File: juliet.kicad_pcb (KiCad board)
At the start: 2 copper layers, 285.4 x 94.9 mm, 143 parts, among them J1 USB, J2 AVR_ISP_6, J3 JST, SW1 RESET, SW2 BOOT, U1 ATMEGA328-PU, Y1 16MHz

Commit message: Change bottom row layout options
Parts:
- removed 1.5u2_MX43: RCtrl, juliet:MX_PCB_150H
- added 1u_MX30: Fn2, juliet:MX, F.Cu at (147.6, 140.5)
- added 1u_MX37: Fn3, juliet:MX, F.Cu at (209.6, 140.5)
- added 2.25u_MX36: RSpace, juliet:MX_PCB_225H, F.Cu at (178.6, 140.5)
- added D37: 1N4148, Diode_THT:D_DO-35_SOD27_P7.62mm_Horizontal, F.Cu at (219.1, 135.7)
- added OSHW: OSHW-Logo_7.5x8mm_Copper, Symbol:OSHW-Logo_7.5x8mm_Copper, F.Cu at (85.7, 140.5)
- 1.5u_MX46: value Back -> Backspace
- 1u_MX36: value Fn1 -> Fn2
- 1u_MX44: value RAlt -> Down
- 1u_MX50: value RGui -> Up
- 1u_MX51: value RCtrl -> Right
- J1: footprint lumberjack:USB_Hybrid_THT -> juliet:USB_Hybrid_THT
- moved H2 2.38 mm to (152.4, 69.1)
- moved H9 2.15 mm to (293.8, 111.4)
- moved H4 1.91 mm to (11.2, 111.4)
- moved J3 1.90 mm to (103.6, 63.8)
- moved LED2 1.78 mm to (281.0, 66.7)
- moved R6 0.99 mm to (32.0, 70.0)
- moved C2 0.79 mm to (122.8, 69.2)
- moved C1 0.75 mm to (137.2, 69.2)
- moved R5 0.63 mm to (32.0, 67.9)
- moved Y1 0.59 mm to (127.5, 70.5)
- moved J2 0.58 mm to (191.5, 71.2)
- moved F1 0.54 mm to (105.0, 71.0)
- moved H1 0.24 mm to (14.5, 59.5)
- moved H3 0.24 mm to (290.3, 59.5)
- renumbered REF** to Flags
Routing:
- net /ROW6: track 172.6 -> 283.4 mm
- net /COL5: track 190.5 -> 219.0 mm
- net Net-(1.5u_MX43-Pad2): track 98.0 -> 76.3 mm
- net Net-(1u_MX36-Pad1): track 87.8 -> 107.1 mm
- net /COL4: track 148.5 -> 163.3 mm
- net GND: track 16.7 -> 30.3 mm
- net Net-(1u_MX37-Pad1): track 0.00 -> 10.8 mm
- net /COL6: track 274.1 -> 265.1 mm
- net Net-(D61-Pad1): track 157.9 -> 156.3 mm
- net Net-(1.75u_MX42-Pad2): track 56.9 -> 58.1 mm
- net Net-(D62-Pad1): track 166.5 -> 165.5 mm
- net Net-(J1-PadCC2): track 20.1 -> 19.1 mm
- net /RESET: track 95.2 -> 94.4 mm
- net /ROW3: track 240.2 -> 239.4 mm
- net Net-(F1-Pad1): track 102.2 -> 103.0 mm
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
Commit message: Switch bottom row stabilizer orientation
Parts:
- 2.25u_MX30, 2.25u_MX36: footprint juliet:MX_PCB_225H -> juliet:MX_PCB_225B
- 2.75u_MX18: footprint juliet:MX_PCB_275H -> juliet:MX_PCB_275B
- moved D62 0.23 mm to (168.6, 58.6)
- moved D61 0.22 mm to (168.6, 61.0)
- moved R2 0.21 mm to (168.6, 69.5)
- moved R1 0.21 mm to (176.2, 72.0)
- moved R3 0.09 mm to (176.2, 67.0)
- moved R4 0.09 mm to (168.6, 64.5)
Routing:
- net Net-(D62-Pad1): track 165.5 -> 166.1 mm

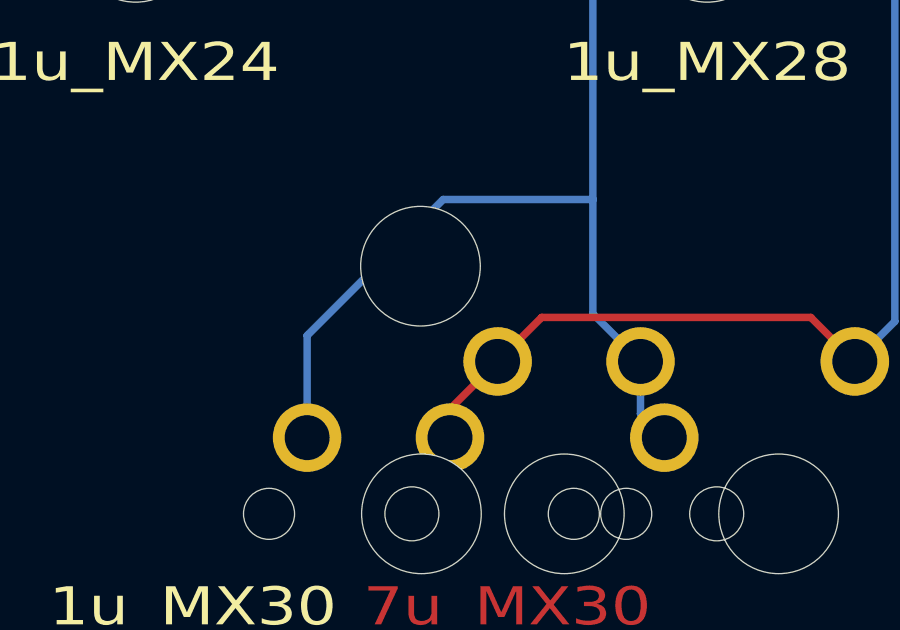
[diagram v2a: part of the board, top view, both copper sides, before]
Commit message: Fix overlapping trace on MX30
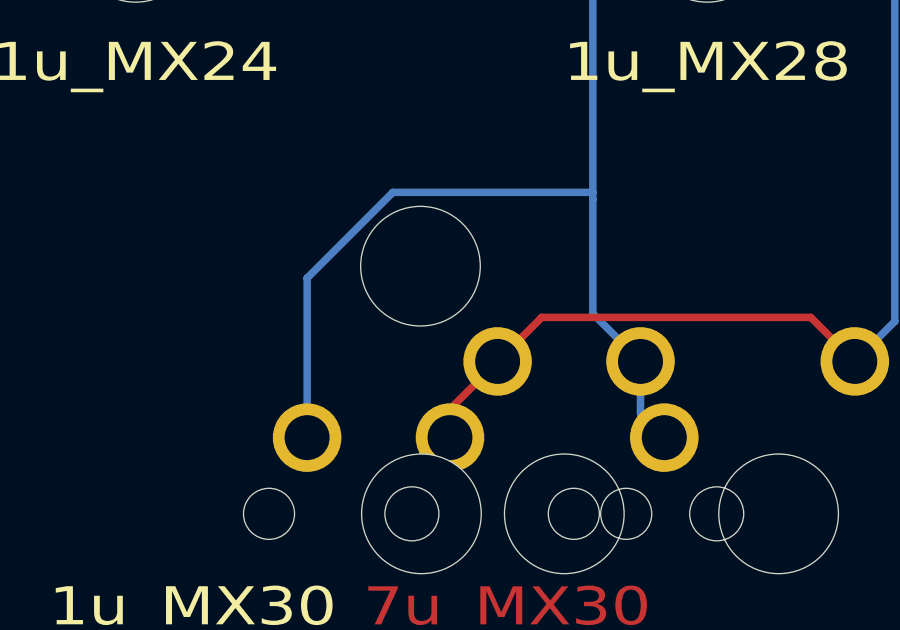
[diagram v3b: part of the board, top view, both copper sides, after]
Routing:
- net /COL4: track 163.3 -> 164.6 mm
